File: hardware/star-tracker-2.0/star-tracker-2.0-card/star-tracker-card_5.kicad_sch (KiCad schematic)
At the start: 21 parts, among them Q6 MMBT2907, U7 OSD3358-512M-BSM, U8 SN74LVC1G07DCK, U9 TLVH431

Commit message: Added extra Testpoints
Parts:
- removed TP18: TEST-POINT3X4, oresat-misc:TestPoint_Pad_D1.0mm, symbol oresat-misc:Test-Point-1mm-round
- added TP54: TEST-POINT, star-tracker-card:2MM-TEST-POINT, symbol star-tracker-card-eagle-import:TEST-POINT
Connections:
- net VDD: now also TP54.1
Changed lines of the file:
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@@
-	)
-	(symbol
-		(lib_id "oresat-misc:Test-Point-1mm-round")
-		(at 252.73 54.61 90)
-		(unit 1)
-		(body_style 1)
-		(exclude_from_sim yes)
-		(in_bom no)
-		(on_board yes)
-		(in_pos_files yes)
-		(dnp no)
-		(property "Reference" "TP18"
-			(at 255.27 50.8 90)
-			(show_name no)
-			(do_not_autoplace no)
-			(effects
-				(font
-					(size 1.27 1.27)
-				)
-				(justify left bottom)
-			)
-		)
-		(property "Value" "TEST-POINT3X4"
-			(at 255.27 57.15 0)
-			(hide yes)
-			(show_name no)
-			(do_not_autoplace no)
-			(effects
-				(font
-					(size 1.27 1.27)
-				)
-				(justify left bottom)
-			)
-		)
-		(property "Footprint" "oresat-misc:TestPoint_Pad_D1.0mm"
-			(at 242.57 54.61 0)
-			(hide yes)
-			(show_name no)
-			(do_not_autoplace no)
-			(effects
-				(font
-					(size 1.27 1.27)
-				)
-			)
-		)
-		(property "Datasheet" ""
-			(at 252.73 54.61 0)
-			(hide yes)
-			(show_name no)
-			(do_not_autoplace no)
-			(effects
-				(font
-					(size 1.27 1.27)
-				)
-			)
-		)
-		(property "Description" "1mm round SMT test point"
-			(at 252.73 54.61 0)
-			(hide yes)
-			(show_name no)
-			(do_not_autoplace no)
-			(effects
-				(font
-					(size 1.27 1.27)
-				)
-			)
-		)
-		(pin "1"
-		)
-		(instances
-			(project "star-tracker-card"
-				(path "/324e9eb5-7420-4b7e-862c-cc20bb28618a/27f3aeed-347f-4362-9166-18725d92163b"
-					(reference "TP18")
-					(unit 1)
-				)
-			)
-		)
 	)
 	(symbol
@@
 				(path "/324e9eb5-7420-4b7e-862c-cc20bb28618a/27f3aeed-347f-4362-9166-18725d92163b"
 					(reference "C21")
-					(unit 1)
-				)
-			)
-		)
-	)
-	(symbol
-		(lib_id "star-tracker-card-eagle-import:5V")
-		(at 143.51 49.53 0)
-		(unit 1)
-		(body_style 1)
-		(exclude_from_sim no)
-		(in_bom yes)
-		(on_board yes)
-		(in_pos_files yes)
-		(dnp no)
-		(property "Reference" "#3V-04"
-			(at 143.51 49.53 0)
-			(hide yes)
-			(show_name no)
-			(do_not_autoplace no)
-			(effects
-				(font
-					(size 1.27 1.27)
-				)
-			)
-		)
-		(property "Value" "5V"
-			(at 142.875 48.895 0)
-			(show_name no)
-			(do_not_autoplace no)
-			(effects
-				(font
-					(size 1.27 1.27)
-				)
-				(justify left bottom)
-			)
-		)
-		(property "Footprint" ""
-			(at 143.51 49.53 0)
-			(hide yes)
-			(show_name no)
-			(do_not_autoplace no)
-			(effects
-				(font
-					(size 1.27 1.27)
-				)
-			)
-		)
-		(property "Datasheet" ""
-			(at 143.51 49.53 0)
-			(hide yes)
-			(show_name no)
-			(do_not_autoplace no)
-			(effects
-				(font
-					(size 1.27 1.27)
-				)
-			)
-		)
-		(property "Description" ""
-			(at 143.51 49.53 0)
-			(hide yes)
-			(show_name no)
-			(do_not_autoplace no)
-			(effects
-				(font
-					(size 1.27 1.27)
-				)
-			)
-		)
-		(pin "1"
-		)
-		(instances
-			(project "star-tracker-card"
-				(path "/324e9eb5-7420-4b7e-862c-cc20bb28618a/27f3aeed-347f-4362-9166-18725d92163b"
-					(reference "#3V-04")
 					(unit 1)
 				)
@@
 	)
 	(symbol
+		(lib_id "star-tracker-card-eagle-import:VDD")
+		(at 143.51 52.07 0)
+		(unit 1)
+		(body_style 1)
+		(exclude_from_sim no)
+		(in_bom yes)
+		(on_board yes)
+		(in_pos_files yes)
+		(dnp no)
+		(property "Reference" "#SUPPLY02"
+			(at 143.51 52.07 0)
+			(hide yes)
+			(show_name no)
+			(do_not_autoplace no)
+			(effects
+				(font
+					(size 1.27 1.27)
+				)
+			)
+		)
+		(property "Value" "5V"
+			(at 143.51 49.276 0)
+			(show_name no)
+			(do_not_autoplace no)
+			(effects
+				(font
+					(size 1.27 1.27)
+				)
+				(justify bottom)
+			)
+		)
+		(property "Footprint" ""
+			(at 143.51 52.07 0)
+			(hide yes)
+			(show_name no)
+			(do_not_autoplace no)
+			(effects
+				(font
+					(size 1.27 1.27)
+				)
+			)
+		)
+		(property "Datasheet" ""
+			(at 143.51 52.07 0)
+			(hide yes)
+			(show_name no)
+			(do_not_autoplace no)
+			(effects
+				(font
+					(size 1.27 1.27)
+				)
+			)
+		)
+		(property "Description" ""
+			(at 143.51 52.07 0)
+			(hide yes)
+			(show_name no)
+			(do_not_autoplace no)
+			(effects
+				(font
+					(size 1.27 1.27)
+				)
+			)
+		)
+		(pin "1"
+		)
+		(instances
+			(project "star-tracker-card"
+				(path "/324e9eb5-7420-4b7e-862c-cc20bb28618a/27f3aeed-347f-4362-9166-18725d92163b"
+					(reference "#SUPPLY02")
+					(unit 1)
+				)
+			)
+		)
+	)
+	(symbol
 		(lib_id "oresat-misc:Test-Point-1mm-round")
 		(at 280.67 217.17 90)
@@
 					(unit 1)
 				)
+			)
+		)
+	)
+	(symbol
+		(lib_id "star-tracker-card-eagle-import:TEST-POINT")
+		(at 252.73 54.61 180)
+		(unit 1)
+		(body_style 1)
+		(exclude_from_sim no)
+		(in_bom no)
+		(on_board yes)
+		(in_pos_files yes)
+		(dnp no)
+		(property "Reference" "TP54"
+			(at 255.27 50.8 0)
+			(show_name no)
+			(do_not_autoplace no)
+			(effects
+				(font
+					(size 1.27 1.27)
+				)
+				(justify left bottom)
+			)
+		)
+		(property "Value" "TEST-POINT"
+			(at 252.73 54.61 0)
+			(hide yes)
+			(show_name no)
+			(do_not_autoplace no)
+			(effects
+				(font
+					(size 1.27 1.27)
+				)
+			)
+		)
+		(property "Footprint" "star-tracker-card:2MM-TEST-POINT"
+			(at 252.73 54.61 0)
+			(hide yes)
+			(show_name no)
+			(do_not_autoplace no)
+			(effects
+				(font
+					(size 1.27 1.27)
+				)
+			)
+		)
+		(property "Datasheet" ""
+			(at 252.73 54.61 0)
+			(hide yes)
+			(show_name no)
+			(do_not_autoplace no)
+			(effects
+				(font
+					(size 1.27 1.27)
+				)
+			)
+		)
+		(property "Description" ""
+			(at 252.73 54.61 0)
+			(hide yes)
+			(show_name no)
+			(do_not_autoplace no)
+			(effects
+				(font
+					(size 1.27 1.27)
+				)
+			)
+		)
+		(pin "1"
+		)
+		(instances
+			(project "star-tracker-card"
+				(path "/324e9eb5-7420-4b7e-862c-cc20bb28618a/27f3aeed-347f-4362-9166-18725d92163b"
+					(reference "TP54")
+					(unit 1)
+				)

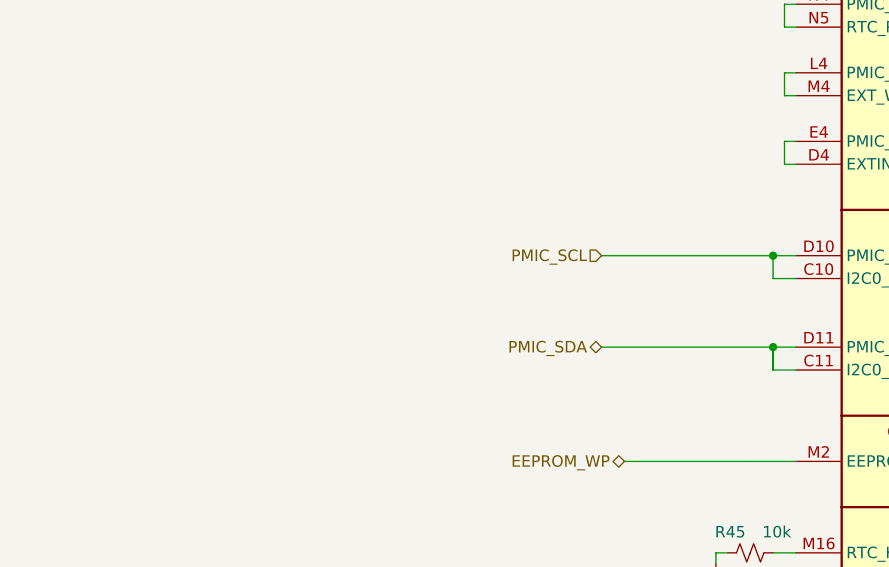
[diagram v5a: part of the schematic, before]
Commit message: Update
changed IMU to I2C bus 1, instead of shared bus 2 with the i2c camera control. Updated IMU interrupt pin location.
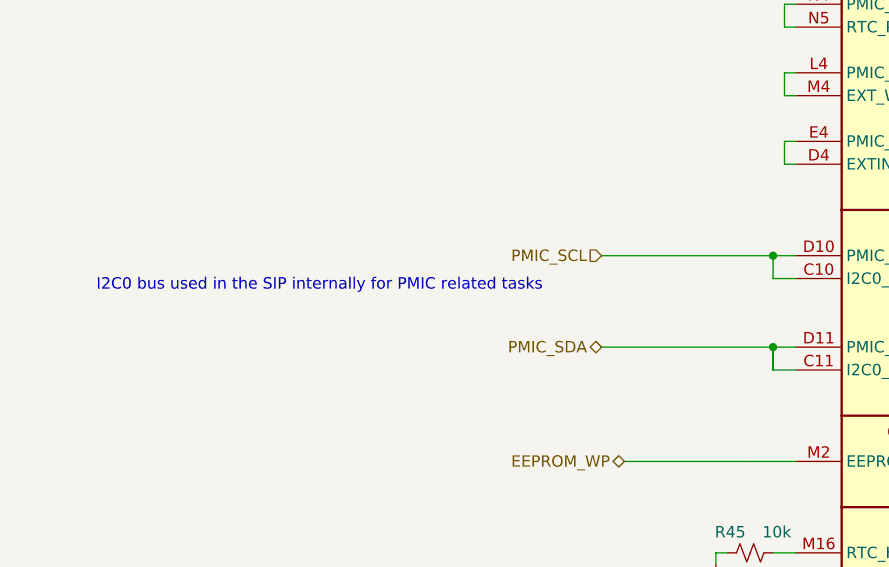
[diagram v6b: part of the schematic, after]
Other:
- note added: "I2C0 bus used in the SIP internally for PMIC related tasks"
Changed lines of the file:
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@@
+		)
+	)
+	(text "I2C0 bus used in the SIP internally for PMIC related tasks\n"
+		(exclude_from_sim no)
+		(at 96.266 188.214 0)
+		(effects
+			(font
+				(size 1.27 1.27)
+			)
+			(justify left bottom)
 		)
 	)
